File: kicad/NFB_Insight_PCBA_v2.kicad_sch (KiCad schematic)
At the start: 0 parts

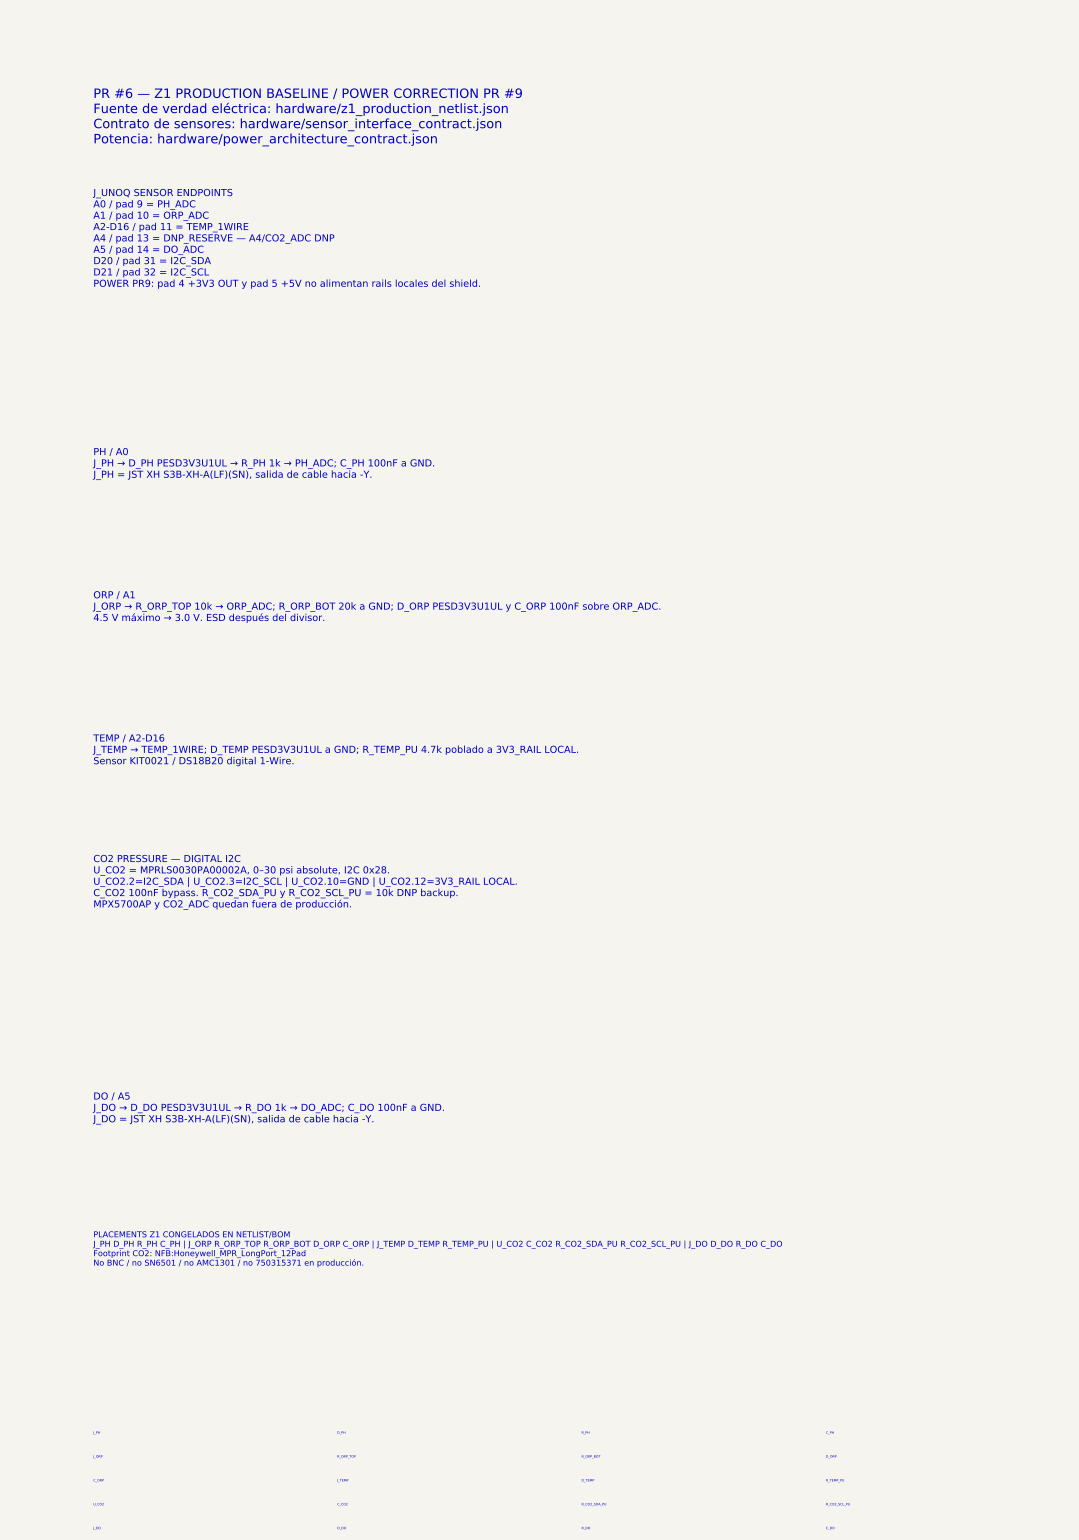
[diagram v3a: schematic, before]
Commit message: actuadores: congelar Z4 protegido y diagnosticable para Insight (#12)
Sustituye etapas legacy por DRV8242H-Q1, TPS1HC120C-Q1 y PhotoMOS AQY212EHAX; añade telemetría de bomba en A4, diagnóstico común D10, SELV/no-mains para chiller y gates Z4 con 10/10 checks verdes.
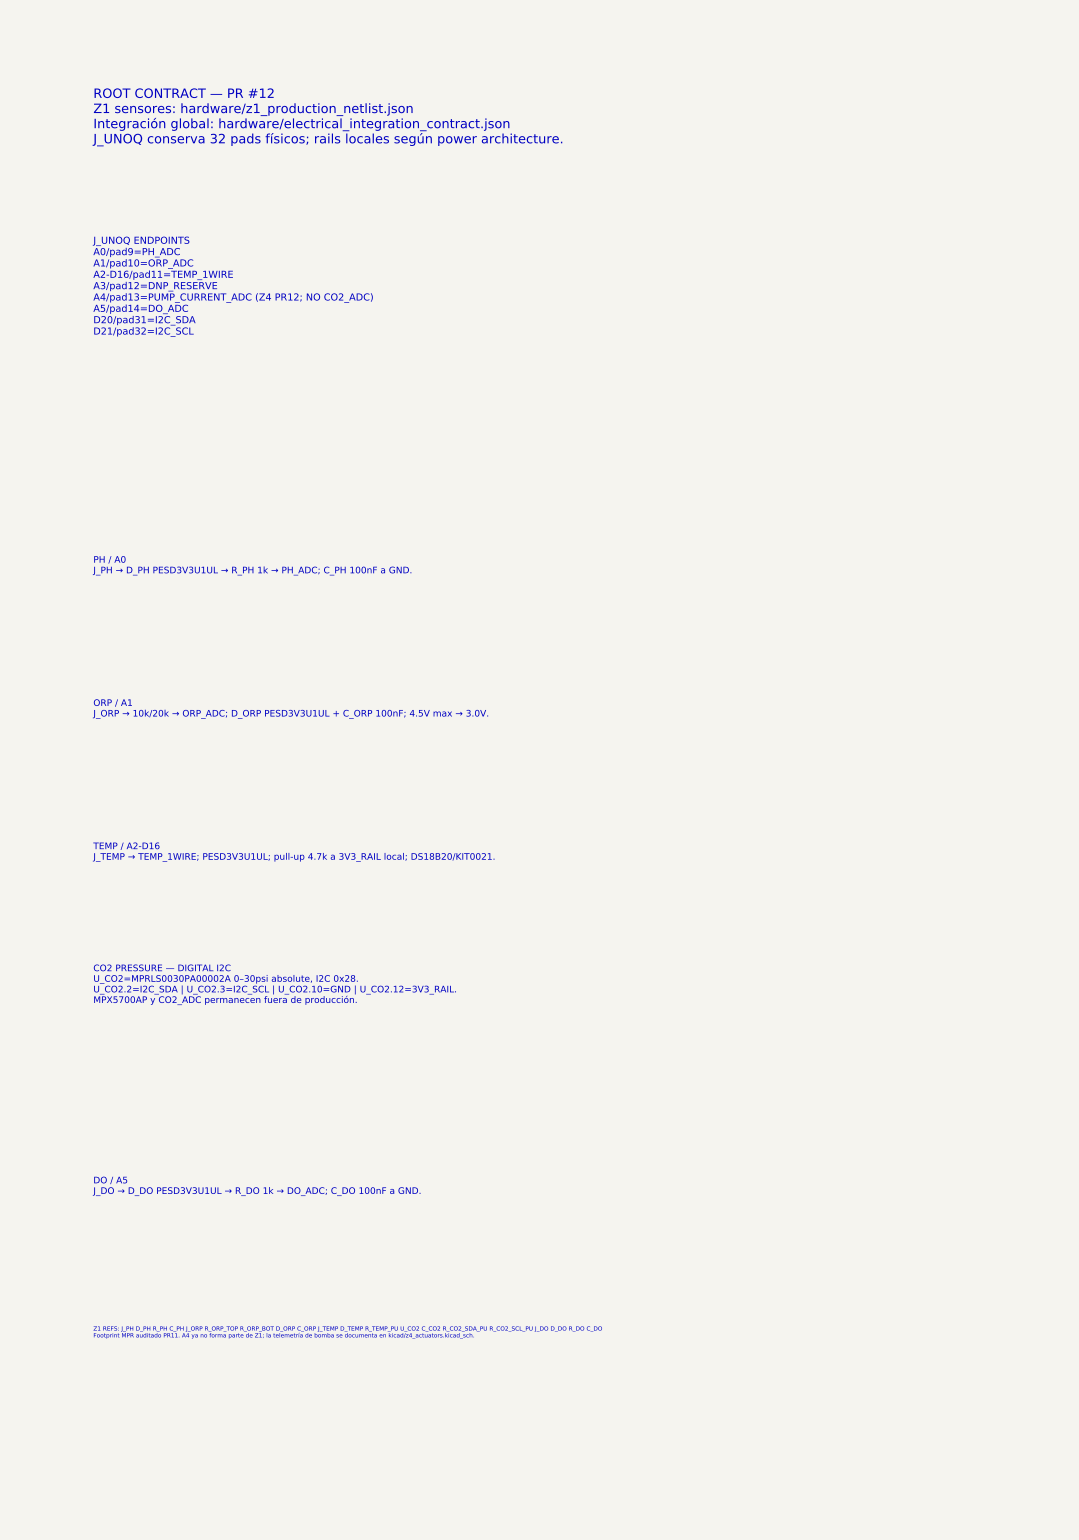
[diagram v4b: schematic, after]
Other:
- note added: "CO2 PRESSURE — DIGITAL I2C U_CO2=MPRLS0030PA00002A 0–30psi absolute, I2C 0x28. U_CO2.2=I2C_SDA | U_CO2.3=I2C_SCL | U_CO2.10=GND | U_CO2.12=3V3_RAIL. MPX5700AP y CO2_ADC permanecen fuera de producción."
- note added: "DO / A5 J_DO → D_DO PESD3V3U1UL → R_DO 1k → DO_ADC; C_DO 100nF a GND."
- note added: "J_UNOQ ENDPOINTS A0/pad9=PH_ADC A1/pad10=ORP_ADC A2-D16/pad11=TEMP_1WIRE A3/pad12=DNP_RESERVE A4/pad13=PUMP_CURRENT_ADC (Z4 PR12; NO CO2_ADC) A5/pad14=DO_ADC D20/pad31=I2C_SDA D21/pad32=I2C_SCL"
- note added: "ORP / A1 J_ORP → 10k/20k → ORP_ADC; D_ORP PESD3V3U1UL + C_ORP 100nF; 4.5V max → 3.0V."
- note added: "PH / A0 J_PH → D_PH PESD3V3U1UL → R_PH 1k → PH_ADC; C_PH 100nF a GND."
- note added: "ROOT CONTRACT — PR #12 Z1 sensores: hardware/z1_production_netlist.json Integración global: hardware/electrical_integration_contract.json J_UNOQ conserva 32 pads físicos; rails locales según power architecture."
- note added: "TEMP / A2-D16 J_TEMP → TEMP_1WIRE; PESD3V3U1UL; pull-up 4.7k a 3V3_RAIL local; DS18B20/KIT0021."
- note added: "Z1 REFS: J_PH D_PH R_PH C_PH J_ORP R_ORP_TOP R_ORP_BOT D_ORP C_ORP J_TEMP D_TEMP R_TEMP_PU U_CO2 C_CO2 R_CO2_SDA_PU R_CO2_SCL_PU J_DO D_DO R_DO C_DO Footprint MPR auditado PR11. A4 ya no forma parte de Z1; la telemetría de bomba se documenta en kicad/z4_actuators.kicad_sch."
- note removed: "CO2 PRESSURE — DIGITAL I2C U_CO2 = MPRLS0030PA00002A, 0–30 psi absolute, I2C 0x28. U_CO2.2=I2C_SDA | U_CO2.3=I2C_SCL | U_CO2.10=GND | U_CO2.12=3V3_RAIL LOCAL. C_CO2 100nF bypass. R_CO2_SDA_PU y R_CO2_SCL_PU = 10k DNP backup. MPX5700AP y CO2_ADC quedan fuera de producción."
- note removed: "C_CO2"
- note removed: "C_DO"
- note removed: "C_ORP"
- note removed: "C_PH"
- note removed: "DO / A5 J_DO → D_DO PESD3V3U1UL → R_DO 1k → DO_ADC; C_DO 100nF a GND. J_DO = JST XH S3B-XH-A(LF)(SN), salida de cable hacia -Y."
- note removed: "D_DO"
- note removed: "D_ORP"
- note removed: "D_PH"
- note removed: "D_TEMP"
- note removed: "J_DO"
- note removed: "J_ORP"
- note removed: "J_PH"
- note removed: "J_TEMP"
- note removed: "J_UNOQ SENSOR ENDPOINTS A0 / pad 9 = PH_ADC A1 / pad 10 = ORP_ADC A2-D16 / pad 11 = TEMP_1WIRE A4 / pad 13 = DNP_RESERVE — A4/CO2_ADC DNP A5 / pad 14 = DO_ADC D20 / pad 31 = I2C_SDA D21 / pad 32 = I2C_SCL POWER PR9: pad 4 +3V3 OUT y pad 5 +5V no alimentan rails locales del shield."
- note removed: "ORP / A1 J_ORP → R_ORP_TOP 10k → ORP_ADC; R_ORP_BOT 20k a GND; D_ORP PESD3V3U1UL y C_ORP 100nF sobre ORP_ADC. 4.5 V máximo → 3.0 V. ESD después del divisor."
- note removed: "PH / A0 J_PH → D_PH PESD3V3U1UL → R_PH 1k → PH_ADC; C_PH 100nF a GND. J_PH = JST XH S3B-XH-A(LF)(SN), salida de cable hacia -Y."
- note removed: "PLACEMENTS Z1 CONGELADOS EN NETLIST/BOM J_PH D_PH R_PH C_PH | J_ORP R_ORP_TOP R_ORP_BOT D_ORP C_ORP | J_TEMP D_TEMP R_TEMP_PU | U_CO2 C_CO2 R_CO2_SDA_PU R_CO2_SCL_PU | J_DO D_DO R_DO C_DO Footprint CO2: NFB:Honeywell_MPR_LongPort_12Pad No BNC / no SN6501 / no AMC1301 / no 750315371 en producción."
- note removed: "PR #6 — Z1 PRODUCTION BASELINE / POWER CORRECTION PR #9 Fuente de verdad eléctrica: hardware/z1_production_netlist.json Contrato de sensores: hardware/sensor_interface_contract.json Potencia: hardware/power_architecture_contract.json"
- note removed: "R_CO2_SCL_PU"
- note removed: "R_CO2_SDA_PU"
- note removed: "R_DO"
- note removed: "R_ORP_BOT"
- note removed: "R_ORP_TOP"
- note removed: "R_PH"
- note removed: "R_TEMP_PU"
- note removed: "TEMP / A2-D16 J_TEMP → TEMP_1WIRE; D_TEMP PESD3V3U1UL a GND; R_TEMP_PU 4.7k poblado a 3V3_RAIL LOCAL. Sensor KIT0021 / DS18B20 digital 1-Wire."
- note removed: "U_CO2"
- title: NFB Insight PCBA v2 — Z1 Sensor Production Contract -> NFB Insight PCBA v2 — Root Contract / Z1 Sensors
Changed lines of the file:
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@@
 (kicad_sch
   (version 20250114)
-  (generator "nfb_pr6_contract")
-  (generator_version "1.5")
+  (generator "nfb_pr12_root_contract")
+  (generator_version "1.0")
   (paper "A3")
   (title_block
-    (title "NFB Insight PCBA v2 — Z1 Sensor Production Contract")
-    (date "2026-08-11")
-    (rev "0.9.0")
+    (title "NFB Insight PCBA v2 — Root Contract / Z1 Sensors")
+    (date "2026-08-12")
+    (rev "0.12.0")
     (company "Cafelium SRL / Nebula Ecosystem")
-    (comment 1 "PR #6 Z1 preservado; frontera de potencia corregida por PR #9")
-    (comment 2 "BOM: bom/insight_z1_production_bom.csv")
-    (comment 3 "A4/CO2_ADC DNP; CO2=MPRLS0030PA00002A I2C 0x28")
-    (comment 4 "5V_RAIL/3V3_RAIL son locales al shield; J_UNOQ.4/.5 no los alimentan")
+    (comment 1 "Z1 PR6 preservado; potencia PR9; footprint MPR PR11; A4 reutilizado por Z4 PR12")
+    (comment 2 "Z1 netlist: hardware/z1_production_netlist.json")
+    (comment 3 "CO2=MPRLS0030PA00002A I2C 0x28; CO2_ADC retirado")
+    (comment 4 "A4/pad13=PUMP_CURRENT_ADC pertenece a Z4, no a Z1")
   )
-  (text "PR #6 — Z1 PRODUCTION BASELINE / POWER CORRECTION PR #9\nFuente de verdad eléctrica: hardware/z1_production_netlist.json\nContrato de sensores: hardware/sensor_interface_contract.json\nPotencia: hardware/power_architecture_contract.json"
+  (text "ROOT CONTRACT — PR #12\nZ1 sensores: hardware/z1_production_netlist.json\nIntegración global: hardware/electrical_integration_contract.json\nJ_UNOQ conserva 32 pads físicos; rails locales según power architecture."
     (exclude_from_sim no)
     (at 38.1 35.56 0)
-    (effects (font (size 2.0 2.0)) (justify left bottom))
+    (effects (font (size 2 2)) (justify left bottom))
   )
-  (text "J_UNOQ SENSOR ENDPOINTS\nA0 / pad 9 = PH_ADC\nA1 / pad 10 = ORP_ADC\nA2-D16 / pad 11 = TEMP_1WIRE\nA4 / pad 13 = DNP_RESERVE — A4/CO2_ADC DNP\nA5 / pad 14 = DO_ADC\nD20 / pad 31 = I2C_SDA\nD21 / pad 32 = I2C_SCL\nPOWER PR9: pad 4 +3V3 OUT y pad 5 +5V no alimentan rails locales del shield."
+  (text "J_UNOQ ENDPOINTS\nA0/pad9=PH_ADC\nA1/pad10=ORP_ADC\nA2-D16/pad11=TEMP_1WIRE\nA3/pad12=DNP_RESERVE\nA4/pad13=PUMP_CURRENT_ADC (Z4 PR12; NO CO2_ADC)\nA5/pad14=DO_ADC\nD20/pad31=I2C_SDA\nD21/pad32=I2C_SCL"
     (exclude_from_sim no)
-    (at 38.1 66.04 0)
+    (at 38.1 76.2 0)
     (effects (font (size 1.5 1.5)) (justify left bottom))
   )
-  (text "PH / A0\nJ_PH → D_PH PESD3V3U1UL → R_PH 1k → PH_ADC; C_PH 100nF a GND.\nJ_PH = JST XH S3B-XH-A(LF)(SN), salida de cable hacia -Y."
+  (text "PH / A0\nJ_PH → D_PH PESD3V3U1UL → R_PH 1k → PH_ADC; C_PH 100nF a GND."
     (exclude_from_sim no)
-    (at 38.1 106.68 0)
-    (effects (font (size 1.5 1.5)) (justify left bottom))
+    (at 38.1 127 0)
+    (effects (font (size 1.4 1.4)) (justify left bottom))
   )
-  (text "ORP / A1\nJ_ORP → R_ORP_TOP 10k → ORP_ADC; R_ORP_BOT 20k a GND; D_ORP PESD3V3U1UL y C_ORP 100nF sobre ORP_ADC.\n4.5 V máximo → 3.0 V. ESD después del divisor."
+  (text "ORP / A1\nJ_ORP → 10k/20k → ORP_ADC; D_ORP PESD3V3U1UL + C_ORP 100nF; 4.5V max → 3.0V."
     (exclude_from_sim no)
-    (at 38.1 137.16 0)
-    (effects (font (size 1.5 1.5)) (justify left bottom))
+    (at 38.1 157.48 0)
+    (effects (font (size 1.4 1.4)) (justify left bottom))
   )
-  (text "TEMP / A2-D16\nJ_TEMP → TEMP_1WIRE; D_TEMP PESD3V3U1UL a GND; R_TEMP_PU 4.7k poblado a 3V3_RAIL LOCAL.\nSensor KIT0021 / DS18B20 digital 1-Wire."
+  (text "TEMP / A2-D16\nJ_TEMP → TEMP_1WIRE; PESD3V3U1UL; pull-up 4.7k a 3V3_RAIL local; DS18B20/KIT0021."
     (exclude_from_sim no)
-    (at 38.1 167.64 0)
-    (effects (font (size 1.5 1.5)) (justify left bottom))
+    (at 38.1 187.96 0)
+    (effects (font (size 1.4 1.4)) (justify left bottom))
   )
-  (text "CO2 PRESSURE — DIGITAL I2C\nU_CO2 = MPRLS0030PA00002A, 0–30 psi absolute, I2C 0x28.\nU_CO2.2=I2C_SDA | U_CO2.3=I2C_SCL | U_CO2.10=GND | U_CO2.12=3V3_RAIL LOCAL.\nC_CO2 100nF bypass. R_CO2_SDA_PU y R_CO2_SCL_PU = 10k DNP backup.\nMPX5700AP y CO2_ADC quedan fuera de producción."
+  (text "CO2 PRESSURE — DIGITAL I2C\nU_CO2=MPRLS0030PA00002A 0–30psi absolute, I2C 0x28.\nU_CO2.2=I2C_SDA | U_CO2.3=I2C_SCL | U_CO2.10=GND | U_CO2.12=3V3_RAIL.\nMPX5700AP y CO2_ADC permanecen fuera de producción."
     (exclude_from_sim no)
-    (at 38.1 198.12 0)
-    (effects (font (size 1.5 1.5)) (justify left bottom))
+    (at 38.1 218.44 0)
+    (effects (font (size 1.4 1.4)) (justify left bottom))
   )
-  (text "DO / A5\nJ_DO → D_DO PESD3V3U1UL → R_DO 1k → DO_ADC; C_DO 100nF a GND.\nJ_DO = JST XH S3B-XH-A(LF)(SN), salida de cable hacia -Y."
+  (text "DO / A5\nJ_DO → D_DO PESD3V3U1UL → R_DO 1k → DO_ADC; C_DO 100nF a GND."
     (exclude_from_sim no)
-    (at 38.1 243.84 0)
-    (effects (font (size 1.5 1.5)) (justify left bottom))
+    (at 38.1 259.08 0)
+    (effects (font (size 1.4 1.4)) (justify left bottom))
   )
-  (text "PLACEMENTS Z1 CONGELADOS EN NETLIST/BOM\nJ_PH D_PH R_PH C_PH | J_ORP R_ORP_TOP R_ORP_BOT D_ORP C_ORP | J_TEMP D_TEMP R_TEMP_PU | U_CO2 C_CO2 R_CO2_SDA_PU R_CO2_SCL_PU | J_DO D_DO R_DO C_DO\nFootprint CO2: NFB:Honeywell_MPR_LongPort_12Pad\nNo BNC / no SN6501 / no AMC1301 / no 750315371 en producción."
+  (text "Z1 REFS: J_PH D_PH R_PH C_PH J_ORP R_ORP_TOP R_ORP_BOT D_ORP C_ORP J_TEMP D_TEMP R_TEMP_PU U_CO2 C_CO2 R_CO2_SDA_PU R_CO2_SCL_PU J_DO D_DO R_DO C_DO\nFootprint MPR auditado PR11. A4 ya no forma parte de Z1; la telemetría de bomba se documenta en kicad/z4_actuators.kicad_sch."
     (exclude_from_sim no)
-    (at 38.1 274.32 0)
-    (effects (font (size 1.25 1.25)) (justify left bottom))
+    (at 38.1 289.56 0)
+    (effects (font (size 0.9 0.9)) (justify left bottom))
   )
-  (text "J_PH" (exclude_from_sim no) (at 38.1 310 0) (effects (font (size 0.5 0.5)) (justify left bottom)))
-  (text "D_PH" (exclude_from_sim no) (at 90 310 0) (effects (font (size 0.5 0.5)) (justify left bottom)))
-  (text "R_PH" (exclude_from_sim no) (at 142 310 0) (effects (font (size 0.5 0.5)) (justify left bottom)))
-  (text "C_PH" (exclude_from_sim no) (at 194 310 0) (effects (font (size 0.5 0.5)) (justify left bottom)))
-  (text "J_ORP" (exclude_from_sim no) (at 38.1 315.08 0) (effects (font (size 0.5 0.5)) (justify left bottom)))
-  (text "R_ORP_TOP" (exclude_from_sim no) (at 90 315.08 0) (effects (font (size 0.5 0.5)) (justify left bottom)))
-  (text "R_ORP_BOT" (exclude_from_sim no) (at 142 315.08 0) (effects (font (size 0.5 0.5)) (justify left bottom)))
-  (text "D_ORP" (exclude_from_sim no) (at 194 315.08 0) (effects (font (size 0.5 0.5)) (justify left bottom)))
-  (text "C_ORP" (exclude_from_sim no) (at 38.1 320.16 0) (effects (font (size 0.5 0.5)) (justify left bottom)))
-  (text "J_TEMP" (exclude_from_sim no) (at 90 320.16 0) (effects (font (size 0.5 0.5)) (justify left bottom)))
-  (text "D_TEMP" (exclude_from_sim no) (at 142 320.16 0) (effects (font (size 0.5 0.5)) (justify left bottom)))
-  (text "R_TEMP_PU" (exclude_from_sim no) (at 194 320.16 0) (effects (font (size 0.5 0.5)) (justify left bottom)))
-  (text "U_CO2" (exclude_from_sim no) (at 38.1 325.24 0) (effects (font (size 0.5 0.5)) (justify left bottom)))
-  (text "C_CO2" (exclude_from_sim no) (at 90 325.24 0) (effects (font (size 0.5 0.5)) (justify left bottom)))
-  (text "R_CO2_SDA_PU" (exclude_from_sim no) (at 142 325.24 0) (effects (font (size 0.5 0.5)) (justify left bottom)))
-  (text "R_CO2_SCL_PU" (exclude_from_sim no) (at 194 325.24 0) (effects (font (size 0.5 0.5)) (justify left bottom)))
-  (text "J_DO" (exclude_from_sim no) (at 38.1 330.32 0) (effects (font (size 0.5 0.5)) (justify left bottom)))
-  (text "D_DO" (exclude_from_sim no) (at 90 330.32 0) (effects (font (size 0.5 0.5)) (justify left bottom)))
-  (text "R_DO" (exclude_from_sim no) (at 142 330.32 0) (effects (font (size 0.5 0.5)) (justify left bottom)))
-  (text "C_DO" (exclude_from_sim no) (at 194 330.32 0) (effects (font (size 0.5 0.5)) (justify left bottom)))
   (sheet_instances
     (path "/" (page "1"))
